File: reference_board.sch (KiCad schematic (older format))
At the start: 2 parts, among them J1 CONN_02X04, U3 AD590

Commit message: Positive zener pin now has a sense connection to correct fot the error caused by the 1 mA zener current Changed zener bias current resistor to less expensive smd precision resistor Added a 2nd parallel resistor to the divider to make fine tuning easier Changed pin layout of the connector (due to the sense connection)
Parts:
- J1: symbol CONN_02X04 -> Conn_02x04_Odd_Even
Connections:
- net labels added: Vout, Zener+_force, Zener+_sense
- wire segments 25 -> 36
- no-connect marks 1 -> 0
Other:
- moved on the sheet: U3
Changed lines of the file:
@@
 LIBS:Linear Technology
 LIBS:ADI
+LIBS:net-tie
 LIBS:reference_board-cache
 EELAYER 26 0
@@
 encoding utf-8
 Sheet 1 2
-Title ""
-Date ""
-Rev ""
+Title "LM399 negative voltage reference"
+Date "2017-09-28"
+Rev "v2.0.1"
 Comp ""
-Comment1 ""
-Comment2 ""
+Comment1 "Copyright (©) 2017, Patrick Baus <patrick.baus@physik.tu-darmstadt.de>"
+Comment2 "Licensed under CERN OHL v.1.2"
 Comment3 ""
 Comment4 ""
 $EndDescr
 $Comp
-L CONN_02X04 J1
-U 1 1 58D2271F
-P 3000 3600
-F 0 "J1" H 3000 3915 50  0000 C CNN
-F 1 "CONN_02X04" H 3000 3824 50  0000 C CNN
-F 2 "Socket_Strips:Socket_Strip_Straight_2x04_Pitch2.54mm" H 3000 2400 50  0001 C CNN
-F 3 "" H 3000 2400 50  0001 C CNN
-	1    3000 3600
-	1    0    0    -1
-$EndComp
-$Comp
 L AD590 U3
 U 1 1 58DBB9E8
-P 2950 4350
-F 0 "U3" H 3078 4446 50  0000 L CNN
-F 1 "AD590" H 3078 4355 50  0000 L CNN
-F 2 "Housings_SOIC:SOIC-8_3.9x4.9mm_Pitch1.27mm" H 2950 4500 50  0001 C CNN
-F 3 "" H 2950 4350 60  0001 C CNN
-F 4 "Analog Devices" H 2950 4350 60  0001 C CNN "MFN"
-F 5 "AD590" H 2950 4350 60  0001 C CNN "MFP"
-	1    2950 4350
+P 2950 4750
+F 0 "U3" H 3078 4846 50  0000 L CNN
+F 1 "AD590" H 3078 4755 50  0000 L CNN
+F 2 "Housings_SOIC:SOIC-8_3.9x4.9mm_Pitch1.27mm" H 2950 4900 50  0001 C CNN
+F 3 "" H 2950 4750 60  0001 C CNN
+F 4 "Analog Devices" H 2950 4750 60  0001 C CNN "MFN"
+F 5 "AD590" H 2950 4750 60  0001 C CNN "MFP"
+	1    2950 4750
 	0    1    1    0
 $EndComp
-Text Notes 2550 5050 0    60   ~ 0
+Text Notes 2550 5450 0    60   ~ 0
 Temperature Sensor:\n1 µA/K\n298.2 µA @ 25 °C
 $Comp
 L GND #PWR01
 U 1 1 58DD20AE
-P 3950 3500
-F 0 "#PWR01" H 3950 3250 50  0001 C CNN
-F 1 "GND" H 3955 3327 50  0000 C CNN
-F 2 "" H 3950 3500 50  0001 C CNN
-F 3 "" H 3950 3500 50  0001 C CNN
-	1    3950 3500
-	1    0    0    -1
+P 1800 3300
+F 0 "#PWR01" H 1800 3050 50  0001 C CNN
+F 1 "GND" H 1805 3127 50  0000 C CNN
+F 2 "" H 1800 3300 50  0001 C CNN
+F 3 "" H 1800 3300 50  0001 C CNN
+	1    1800 3300
+	-1   0    0    -1
 $EndComp
-Text Notes 1600 4450 0    60   ~ 0
+Text Notes 1600 4850 0    60   ~ 0
 Try alternative part:\nTC1047
-NoConn ~ 2750 3450
 $Sheet
-S 4850 3600 1400 700
+S 5750 3600 1700 700
 U 591A50E3
 F0 "Voltage Reference" 60
 F1 "LM399.sch" 60
-F2 "V+" U L 4850 3800 60
-F3 "V-" U L 4850 3950 60
-F4 "V_zener+" U L 4850 3700 60
-F5 "V_zener-" O R 6250 3950 60
+F2 "V+" U L 5750 3800 60
+F3 "V-" U L 5750 3900 60
+F4 "V_zener+_force" U L 5750 3700 60
+F5 "V_zener-" O R 7450 3950 60
+F6 "V_zener+_sense" U R 7450 3700 60
+F7 "V-heater+" U L 5750 4100 60
+F8 "V_heater-" U L 5750 4200 60
 $EndSheet
 Wire Wire Line
 	3250 3550 3800 3550
 Wire Wire Line
-	2750 3550 2600 3550
+	2750 3550 1600 3550
 Wire Wire Line
 	2350 3650 2750 3650
@@
 	2750 3750 2600 3750
 Wire Wire Line
-	3950 3450 3950 3500
+	1800 3250 1800 3300
 Wire Wire Line
-	3950 3450 3250 3450
+	1800 3250 2500 3250
 $Comp
 L PWR_FLAG #FLG02
@@
 	3800 3550 3800 3700
 Wire Wire Line
-	3800 3700 4850 3700
+	3800 3700 5750 3700
 Wire Wire Line
 	3700 3650 3700 3800
 Wire Wire Line
-	3700 3800 4850 3800
+	3700 3800 5750 3800
 Wire Wire Line
-	2350 3650 2350 3950
+	2350 3650 2350 3900
 Wire Wire Line
-	2350 3950 4850 3950
+	2350 3900 5750 3900
 Wire Wire Line
-	2600 3550 2600 3050
+	1600 3550 1600 2650
 Wire Wire Line
-	2600 3050 6450 3050
+	1600 2650 7750 2650
 Wire Wire Line
-	6450 3050 6450 3950
+	7750 2650 7750 3950
 Wire Wire Line
-	6450 3950 6250 3950
+	7750 3950 7450 3950
 Wire Wire Line
 	4200 3550 4200 3800
 Connection ~ 4200 3800
 Wire Wire Line
-	4650 3550 4650 3950
-Connection ~ 4650 3950
+	4650 3550 4650 3900
+Connection ~ 4650 3900
 Wire Wire Line
-	3400 3750 3400 4350
+	3400 3750 3400 4750
 Wire Wire Line
-	3400 4350 3250 4350
+	3400 4750 3250 4750
 Wire Wire Line
-	2600 3750 2600 4350
+	2600 3750 2600 4750
 Wire Wire Line
-	2600 4350 2750 4350
+	2600 4750 2750 4750
 $Comp
 L PWR_FLAG #FLG04
 U 1 1 591A6FAC
-P 3600 3350
-F 0 "#FLG04" H 3600 3425 50  0001 C CNN
-F 1 "PWR_FLAG" H 3600 3524 50  0000 C CNN
-F 2 "" H 3600 3350 50  0001 C CNN
-F 3 "" H 3600 3350 50  0001 C CNN
-	1    3600 3350
+P 2150 3150
+F 0 "#FLG04" H 2150 3225 50  0001 C CNN
+F 1 "PWR_FLAG" H 2150 3324 50  0000 C CNN
+F 2 "" H 2150 3150 50  0001 C CNN
+F 3 "" H 2150 3150 50  0001 C CNN
+	1    2150 3150
+	-1   0    0    -1
+$EndComp
+Wire Wire Line
+	2150 3150 2150 3250
+Connection ~ 2150 3250
+$Comp
+L Conn_02x04_Odd_Even J1
+U 1 1 58D2271F
+P 2950 3550
+F 0 "J1" H 2950 3865 50  0000 C CNN
+F 1 "CONN_02X04" H 2950 3774 50  0000 C CNN
+F 2 "Socket_Strips:Socket_Strip_Straight_2x04_Pitch2.54mm" H 2950 2350 50  0001 C CNN
+F 3 "" H 2950 2350 50  0001 C CNN
+	1    2950 3550
 	1    0    0    -1
 $EndComp
 Wire Wire Line
-	3600 3350 3600 3450
-Connection ~ 3600 3450
+	2750 3450 2500 3450
+Wire Wire Line
+	2500 3450 2500 3250
+Wire Wire Line
+	7450 3700 7650 3700
+Wire Wire Line
+	7650 3700 7650 3100
+Wire Wire Line
+	7650 3100 3550 3100
+Wire Wire Line
+	3550 3100 3550 3450
+Wire Wire Line
+	3550 3450 3250 3450
+Text Label 4900 3700 0    60   ~ 0
+Zener+_force
+Text Label 5350 3100 0    60   ~ 0
+Zener+_sense
+Text Label 5700 2650 0    60   ~ 0
+Vout
+Wire Wire Line
+	5050 3800 5050 4100
+Wire Wire Line
+	5050 4100 5750 4100
+Connection ~ 5050 3800
+Wire Wire Line
+	5250 3900 5250 4200
+Wire Wire Line
+	5250 4200 5750 4200
+Connection ~ 5250 3900
 $EndSCHEMATC

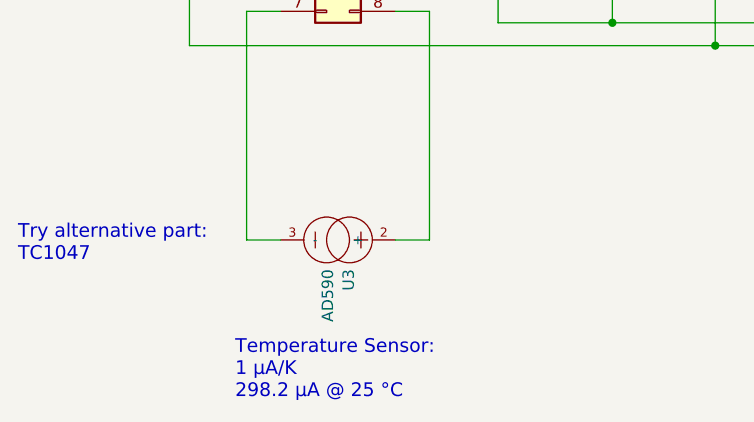
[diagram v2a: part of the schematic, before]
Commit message: Updated picture Updated annotations
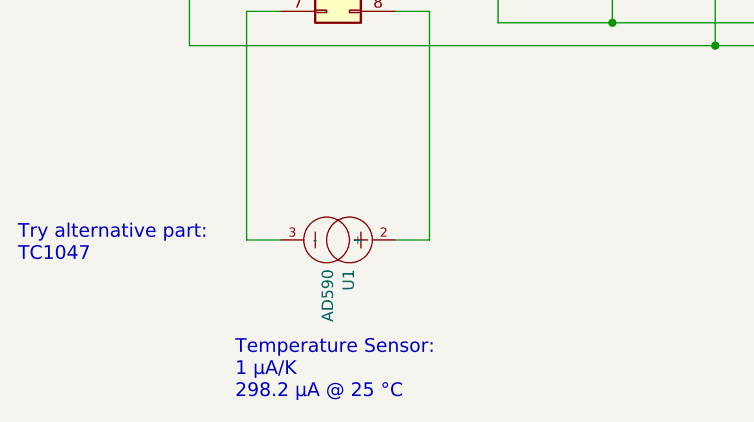
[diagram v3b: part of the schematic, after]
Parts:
- renumbered U3 to U1
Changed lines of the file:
@@
 $EndDescr
 $Comp
-L AD590 U3
+L AD590 U1
 U 1 1 58DBB9E8
 P 2950 4750
-F 0 "U3" H 3078 4846 50  0000 L CNN
+F 0 "U1" H 3078 4846 50  0000 L CNN
 F 1 "AD590" H 3078 4755 50  0000 L CNN
 F 2 "Housings_SOIC:SOIC-8_3.9x4.9mm_Pitch1.27mm" H 2950 4900 50  0001 C CNN
@@
 Temperature Sensor:\n1 µA/K\n298.2 µA @ 25 °C
 $Comp
-L GND #PWR01
+L GND #PWR1
 U 1 1 58DD20AE
 P 1800 3300
-F 0 "#PWR01" H 1800 3050 50  0001 C CNN
+F 0 "#PWR1" H 1800 3050 50  0001 C CNN
 F 1 "GND" H 1805 3127 50  0000 C CNN
 F 2 "" H 1800 3300 50  0001 C CNN
@@
 	1800 3250 2500 3250
 $Comp
-L PWR_FLAG #FLG02
+L PWR_FLAG #FLG3
 U 1 1 591A4DCA
 P 4650 3550
-F 0 "#FLG02" H 4650 3625 50  0001 C CNN
+F 0 "#FLG3" H 4650 3625 50  0001 C CNN
 F 1 "PWR_FLAG" H 4650 3724 50  0000 C CNN
 F 2 "" H 4650 3550 50  0001 C CNN
@@
 $EndComp
 $Comp
-L PWR_FLAG #FLG03
+L PWR_FLAG #FLG2
 U 1 1 591A4CD6
 P 4200 3550
-F 0 "#FLG03" H 4200 3625 50  0001 C CNN
+F 0 "#FLG2" H 4200 3625 50  0001 C CNN
 F 1 "PWR_FLAG" H 4200 3724 50  0000 C CNN
 F 2 "" H 4200 3550 50  0001 C CNN
@@
 	2600 4750 2750 4750
 $Comp
-L PWR_FLAG #FLG04
+L PWR_FLAG #FLG1
 U 1 1 591A6FAC
 P 2150 3150
-F 0 "#FLG04" H 2150 3225 50  0001 C CNN
+F 0 "#FLG1" H 2150 3225 50  0001 C CNN
 F 1 "PWR_FLAG" H 2150 3324 50  0000 C CNN
 F 2 "" H 2150 3150 50  0001 C CNN

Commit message: Updated schematic to KiCAD v5 Reduced board size even further by replacing the AD590 with a TMP236
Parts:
- removed U1: AD590, Housings_SOIC:SOIC-8_3.9x4.9mm_Pitch1.27mm, symbol AD590
- added LOGO1: Logo_Open_Hardware_Small, Symbol:OSHW-Logo2_7.3x6mm_SilkScreen, symbol Graphic:Logo_Open_Hardware_Small
- added U1: TMP236, Package_TO_SOT_SMD:SOT-353_SC-70-5, symbol Sensor_Temperature:TMP20AIDCK
- J1: footprint Socket_Strips:Socket_Strip_Straight_2x04_Pitch2.54mm -> Connector_PinSocket_2.54mm:PinSocket_2x04_P2.54mm_Vertical; symbol Conn_02x04_Odd_Even -> Connector_Generic:Conn_02x04_Odd_Even
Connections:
- wire segments 36 -> 43
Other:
- note added: "3.3V"
- note removed: "Temperature Sensor:\n1 µA/K\n298.2 µA @ 25 °C"
- note removed: "Try alternative part:\nTC1047"
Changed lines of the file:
@@
-EESchema Schematic File Version 2
-LIBS:power
-LIBS:device
-LIBS:transistors
-LIBS:conn
-LIBS:linear
-LIBS:regul
-LIBS:74xx
-LIBS:cmos4000
-LIBS:adc-dac
-LIBS:memory
-LIBS:xilinx
-LIBS:microcontrollers
-LIBS:dsp
-LIBS:microchip
-LIBS:analog_switches
-LIBS:motorola
-LIBS:texas
-LIBS:intel
-LIBS:audio
-LIBS:interface
-LIBS:digital-audio
-LIBS:philips
-LIBS:display
-LIBS:cypress
-LIBS:siliconi
-LIBS:opto
-LIBS:atmel
-LIBS:contrib
-LIBS:valves
-LIBS:Linear Technology
-LIBS:ADI
-LIBS:net-tie
+EESchema Schematic File Version 4
 LIBS:reference_board-cache
 EELAYER 26 0
@@
 Sheet 1 2
 Title "LM399 negative voltage reference"
-Date "2018-01-06"
-Rev "v2.1.0"
+Date "2018-08-17"
+Rev "v2.2.0"
 Comp ""
 Comment1 "Copyright (©) 2018, Patrick Baus <patrick.baus@physik.tu-darmstadt.de>"
@@
 $EndDescr
 $Comp
-L AD590 U1
-U 1 1 58DBB9E8
-P 2950 4750
-F 0 "U1" H 3078 4846 50  0000 L CNN
-F 1 "AD590" H 3078 4755 50  0000 L CNN
-F 2 "Housings_SOIC:SOIC-8_3.9x4.9mm_Pitch1.27mm" H 2950 4900 50  0001 C CNN
-F 3 "" H 2950 4750 60  0001 C CNN
-F 4 "Analog Devices" H 2950 4750 60  0001 C CNN "MFN"
-F 5 "AD590" H 2950 4750 60  0001 C CNN "MFP"
-	1    2950 4750
-	0    1    1    0
-$EndComp
-Text Notes 2550 5450 0    60   ~ 0
-Temperature Sensor:\n1 µA/K\n298.2 µA @ 25 °C
-$Comp
-L GND #PWR1
+L power:GND #PWR01
 U 1 1 58DD20AE
 P 1800 3300
-F 0 "#PWR1" H 1800 3050 50  0001 C CNN
+F 0 "#PWR01" H 1800 3050 50  0001 C CNN
 F 1 "GND" H 1805 3127 50  0000 C CNN
 F 2 "" H 1800 3300 50  0001 C CNN
@@
 	-1   0    0    -1
 $EndComp
-Text Notes 1600 4850 0    60   ~ 0
-Try alternative part:\nTC1047
 $Sheet
 S 5750 3600 1700 700
@@
 	3400 3750 3250 3750
 Wire Wire Line
-	2750 3750 2600 3750
-Wire Wire Line
 	1800 3250 1800 3300
 Wire Wire Line
-	1800 3250 2500 3250
-$Comp
-L PWR_FLAG #FLG3
+	1800 3250 2150 3250
+$Comp
+L power:PWR_FLAG #FLG03
 U 1 1 591A4DCA
 P 4650 3550
-F 0 "#FLG3" H 4650 3625 50  0001 C CNN
+F 0 "#FLG03" H 4650 3625 50  0001 C CNN
 F 1 "PWR_FLAG" H 4650 3724 50  0000 C CNN
 F 2 "" H 4650 3550 50  0001 C CNN
@@
 $EndComp
 $Comp
-L PWR_FLAG #FLG2
+L power:PWR_FLAG #FLG02
 U 1 1 591A4CD6
 P 4200 3550
-F 0 "#FLG2" H 4200 3625 50  0001 C CNN
+F 0 "#FLG02" H 4200 3625 50  0001 C CNN
 F 1 "PWR_FLAG" H 4200 3724 50  0000 C CNN
 F 2 "" H 4200 3550 50  0001 C CNN
@@
 	3700 3650 3700 3800
 Wire Wire Line
-	3700 3800 5750 3800
+	3700 3800 4200 3800
 Wire Wire Line
 	2350 3650 2350 3900
 Wire Wire Line
-	2350 3900 5750 3900
+	2350 3900 4650 3900
 Wire Wire Line
 	1600 3550 1600 2650
@@
 	4650 3550 4650 3900
 Connection ~ 4650 3900
-Wire Wire Line
-	3400 3750 3400 4750
-Wire Wire Line
-	3400 4750 3250 4750
-Wire Wire Line
-	2600 3750 2600 4750
-Wire Wire Line
-	2600 4750 2750 4750
-$Comp
-L PWR_FLAG #FLG1
+$Comp
+L power:PWR_FLAG #FLG01
 U 1 1 591A6FAC
 P 2150 3150
-F 0 "#FLG1" H 2150 3225 50  0001 C CNN
+F 0 "#FLG01" H 2150 3225 50  0001 C CNN
 F 1 "PWR_FLAG" H 2150 3324 50  0000 C CNN
 F 2 "" H 2150 3150 50  0001 C CNN
@@
 Connection ~ 2150 3250
 $Comp
-L Conn_02x04_Odd_Even J1
+L Connector_Generic:Conn_02x04_Odd_Even J1
 U 1 1 58D2271F
 P 2950 3550
 F 0 "J1" H 2950 3865 50  0000 C CNN
 F 1 "CONN_02X04" H 2950 3774 50  0000 C CNN
-F 2 "Socket_Strips:Socket_Strip_Straight_2x04_Pitch2.54mm" H 2950 2350 50  0001 C CNN
+F 2 "Connector_PinSocket_2.54mm:PinSocket_2x04_P2.54mm_Vertical" H 2950 2350 50  0001 C CNN
 F 3 "" H 2950 2350 50  0001 C CNN
 	1    2950 3550
@@
 	5250 4200 5750 4200
 Connection ~ 5250 3900
+Wire Wire Line
+	4200 3800 5050 3800
+Wire Wire Line
+	4650 3900 5250 3900
+Wire Wire Line
+	2150 3250 2500 3250
+Wire Wire Line
+	5050 3800 5750 3800
+Wire Wire Line
+	5250 3900 5750 3900
+$Comp
+L Sensor_Temperature:TMP20AIDCK U1
+U 1 1 5B76F0A6
+P 2550 4650
+F 0 "U1" H 2200 4700 50  0000 R CNN
+F 1 "TMP236" H 2200 4650 50  0000 R CNN
+F 2 "Package_TO_SOT_SMD:SOT-353_SC-70-5" H 2550 4250 50  0001 C CNN
+F 3 "http://www.ti.com/lit/ds/symlink/tmp235.pdf" H 2550 4650 50  0001 C CNN
+F 4 "Texas Instruments" H 2550 4650 50  0001 C CNN "MFN"
+F 5 "TMP236A2DCKT" H 2550 4650 50  0001 C CNN "MFP"
+	1    2550 4650
+	1    0    0    -1
+$EndComp
+$Comp
+L power:GND #PWR0101
+U 1 1 5B76F171
+P 2550 5050
+F 0 "#PWR0101" H 2550 4800 50  0001 C CNN
+F 1 "GND" H 2555 4877 50  0000 C CNN
+F 2 "" H 2550 5050 50  0001 C CNN
+F 3 "" H 2550 5050 50  0001 C CNN
+	1    2550 5050
+	-1   0    0    -1
+$EndComp
+Wire Wire Line
+	2550 5050 2550 4950
+Wire Wire Line
+	2550 4350 2550 3750
+Wire Wire Line
+	2550 3750 2650 3750
+Wire Wire Line
+	3400 3750 3400 4650
+Wire Wire Line
+	3400 4650 2950 4650
+$Comp
+L Graphic:Logo_Open_Hardware_Small LOGO1
+U 1 1 5B772A92
+P 10850 6850
+F 0 "LOGO1" H 10850 7125 50  0001 C CNN
+F 1 "Logo_Open_Hardware_Small" H 10850 6625 50  0001 C CNN
+F 2 "Symbol:OSHW-Logo2_7.3x6mm_SilkScreen" H 10850 6850 50  0001 C CNN
+F 3 "~" H 10850 6850 50  0001 C CNN
+	1    10850 6850
+	1    0    0    -1
+$EndComp
+$Comp
+L power:PWR_FLAG #FLG?
+U 1 1 5B7756A4
+P 2650 3150
+F 0 "#FLG?" H 2650 3225 50  0001 C CNN
+F 1 "PWR_FLAG" H 2650 3324 50  0000 C CNN
+F 2 "" H 2650 3150 50  0001 C CNN
+F 3 "" H 2650 3150 50  0001 C CNN
+	1    2650 3150
+	-1   0    0    -1
+$EndComp
+Wire Wire Line
+	2650 3150 2650 3750
+Connection ~ 2650 3750
+Wire Wire Line
+	2650 3750 2750 3750
+Text Notes 2750 3100 0    60   ~ 0
+3.3V
 $EndSCHEMATC

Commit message: Added M2.5 mounting hole Updated to v3.1
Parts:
- added H1: MountingHole, MountingHole:MountingHole_2.7mm_M2.5_DIN965_Pad, symbol Mechanical:MountingHole
- J1: MFN (none) -> Amphenol; MFP (none) -> 87606-804LF
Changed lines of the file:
@@
 Sheet 1 2
 Title "LM399 negative voltage reference"
-Date "2018-10-04"
-Rev "v3.0.0"
+Date "2019-01-11"
+Rev "v3.1.0"
 Comp ""
 Comment1 "Copyright (©) 2018, Patrick Baus <patrick.baus@physik.tu-darmstadt.de>"
@@
 F 2 "Connector_PinSocket_2.54mm:PinSocket_2x04_P2.54mm_Vertical" H 2950 2350 50  0001 C CNN
 F 3 "" H 2950 2350 50  0001 C CNN
+F 4 "Amphenol" H 2950 3550 50  0001 C CNN "MFN"
+F 5 "87606-804LF" H 2950 3550 50  0001 C CNN "MFP"
 	1    2950 3550
 	1    0    0    -1
@@
 Text Notes 2750 3100 0    60   ~ 0
 3.3V
+$Comp
+L Mechanical:MountingHole H1
+U 1 1 5C37ECDE
+P 3150 3000
+F 0 "H1" H 3250 3050 50  0000 L CNN
+F 1 "MountingHole" H 3250 3000 50  0000 L CNN
+F 2 "MountingHole:MountingHole_2.7mm_M2.5_DIN965_Pad" H 3150 3000 50  0001 C CNN
+F 3 "~" H 3150 3000 50  0001 C CNN
+	1    3150 3000
+	1    0    0    -1
+$EndComp
 $EndSCHEMATC
